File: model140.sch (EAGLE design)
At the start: 12 parts

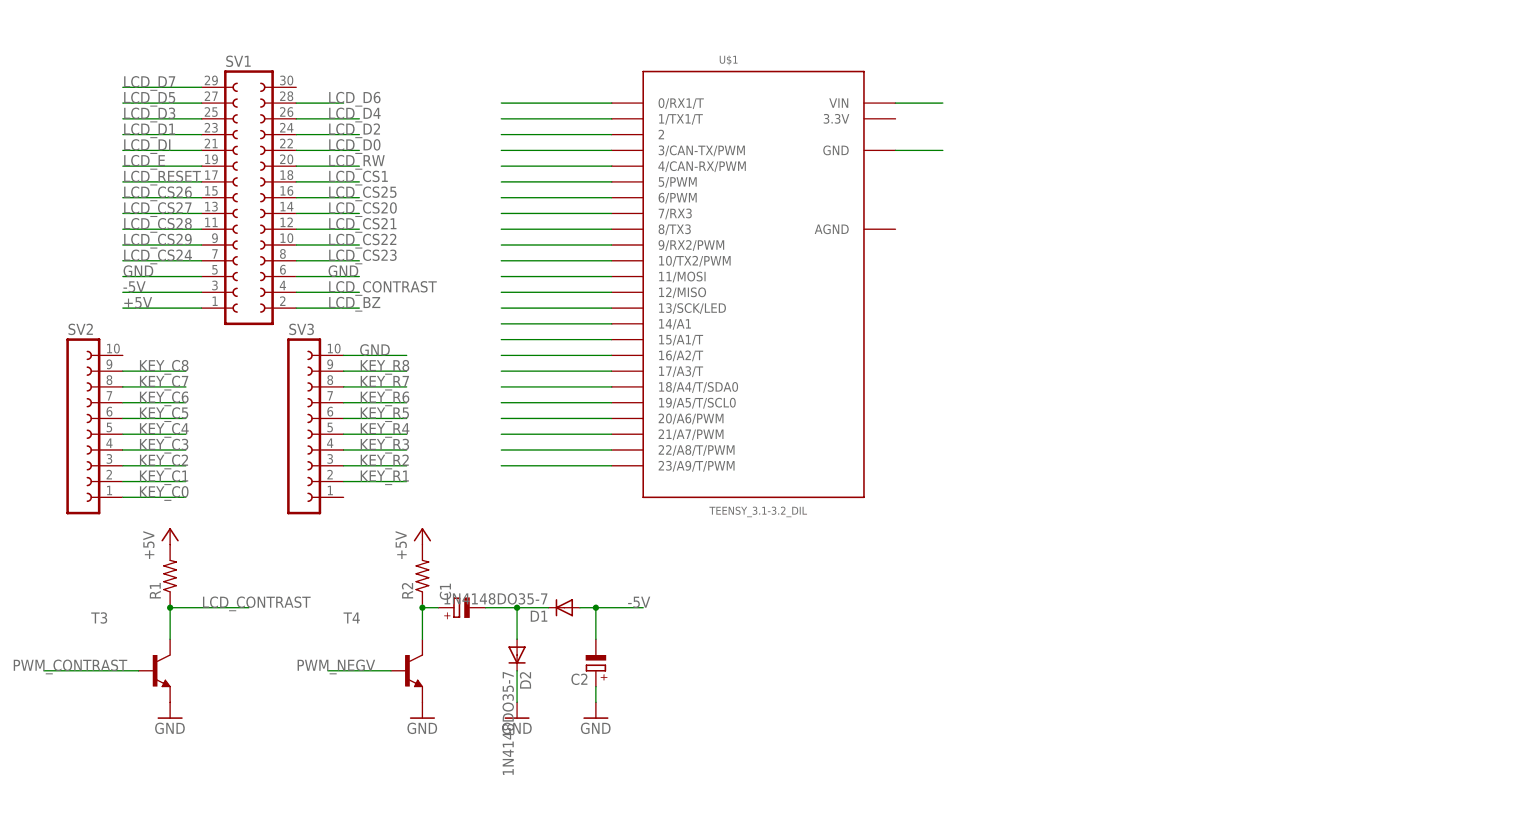
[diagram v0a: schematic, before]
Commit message: pi zero-w version with upduino v2
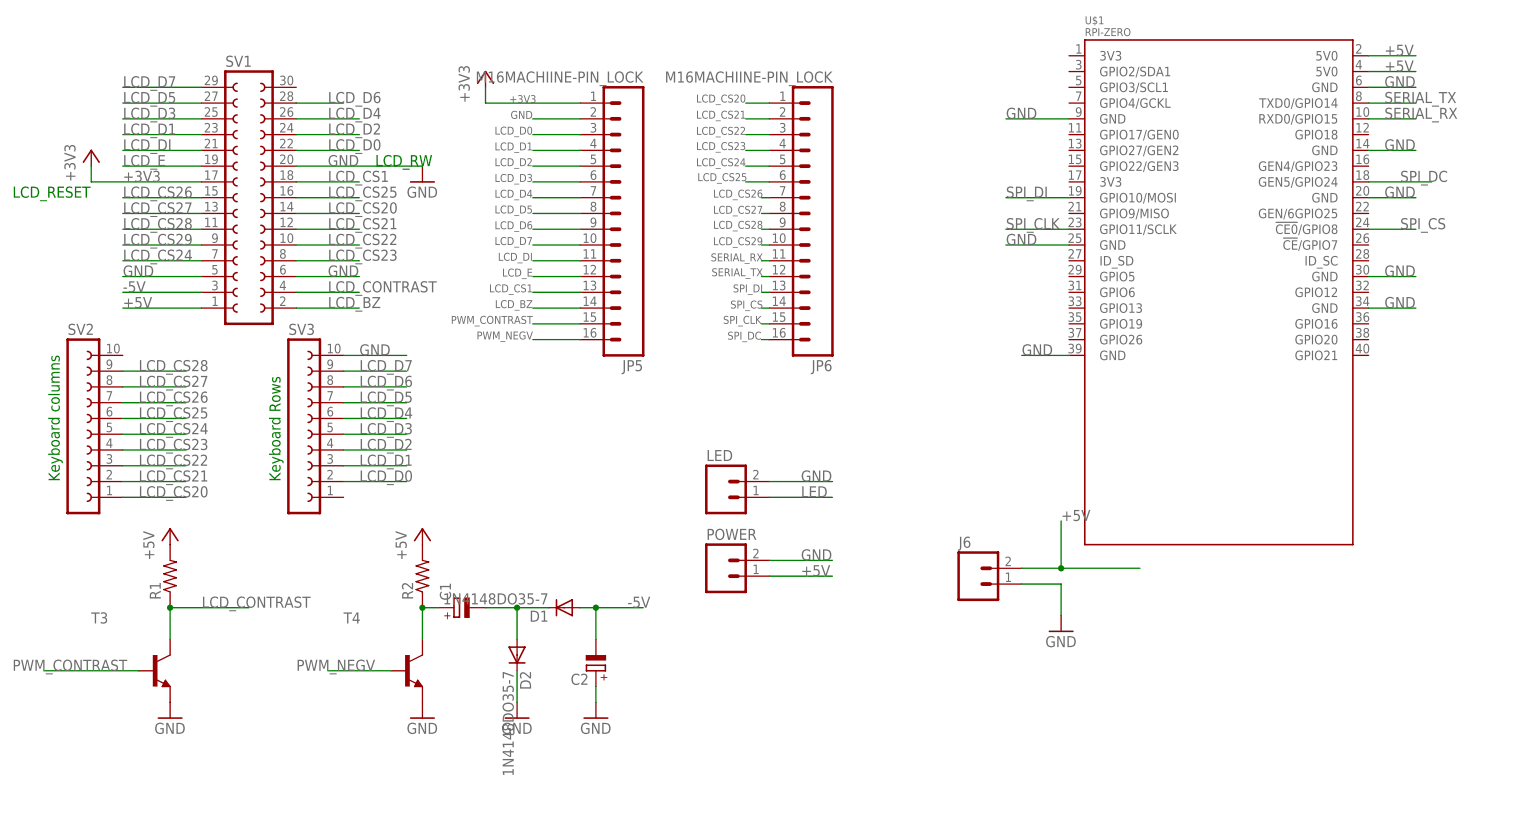
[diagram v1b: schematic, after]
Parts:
- added J6, LED, POWER: (no value), SparkFun-Connectors:M02PTH
- added JP5, JP6: M16MACHIINE-PIN_LOCK, SparkFun-Connectors:M16MACHIINE-PIN_LOCK
- U$1: value TEENSY_3.1-3.2_DIL -> RPI-ZERO; device Teensy_3_and_LC_Series_Boards_v1.4:TEENSY_3.1-3.2_DIL -> rpi-zero:RPI-ZERO
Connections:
- removed net KEY_C0: SV2.1
- removed net KEY_C1: SV2.2
- removed net KEY_C2: SV2.3
- removed net KEY_C3: SV2.4
- removed net KEY_C4: SV2.5
- removed net KEY_C5: SV2.6
- removed net KEY_C6: SV2.7
- removed net KEY_C7: SV2.8
- removed net KEY_C8: SV2.9
- removed net KEY_R1: SV3.2
- removed net KEY_R2: SV3.3
- removed net KEY_R3: SV3.4
- removed net KEY_R4: SV3.5
- removed net KEY_R5: SV3.6
- removed net KEY_R6: SV3.7
- removed net KEY_R7: SV3.8
- removed net KEY_R8: SV3.9
- removed net LCD_RESET: SV1.17
- removed net LCD_RW: SV1.20
- removed net N$1: U$1.0/RX1/T
- removed net N$10: U$1.9/RX2/PWM
- removed net N$11: U$1.10/TX2/PWM
- removed net N$12: U$1.11/MOSI
- removed net N$13: U$1.12/MISO
- removed net N$14: U$1.13/SCK/LED
- removed net N$15: U$1.14/A1
- removed net N$16: U$1.15/A1/T
- removed net N$17: U$1.16/A2/T
- removed net N$18: U$1.17/A3/T
- removed net N$19: U$1.18/A4/T/SDA0
- removed net N$2: U$1.1/TX1/T
- removed net N$20: U$1.19/A5/T/SCL0
- removed net N$21: U$1.20/A6/PWM
- removed net N$22: U$1.21/A7/PWM
- removed net N$23: U$1.22/A8/T/PWM
- removed net N$24: U$1.23/A9/T/PWM
- removed net N$25: U$1.GND
- removed net N$26: U$1.VIN
- removed net N$3: U$1.2
- removed net N$4: U$1.3/CAN-TX/PWM
- removed net N$5: U$1.4/CAN-RX/PWM
- removed net N$6: U$1.5/PWM
- removed net N$7: U$1.6/PWM
- removed net N$8: U$1.7/RX3
- removed net N$9: U$1.8/TX3
- new net +3V3: JP5.1, SV1.17
- new net LED: LED.1
- new net SERIAL_RX: JP6.11, U$1.RXD0/GPIO15
- new net SERIAL_TX: JP6.12, U$1.TXD0/GPIO14
- new net SPI_CLK: JP6.15, U$1.GPIO11/SCLK
- new net SPI_CS: JP6.14, U$1.!CE0!/GPIO8
- new net SPI_DC: JP6.16, U$1.GEN5/GPIO24
- new net SPI_DI: JP6.13, U$1.GPIO10/MOSI
- net +5V: now also J6.2, POWER.1, U$1.5V0@1, U$1.5V0@2
- net GND: now also J6.1, JP5.2, LED.2, POWER.2, SV1.20, U$1.GND@1, U$1.GND@2, U$1.GND@3, U$1.GND@4, U$1.GND@5, U$1.GND@6, U$1.GND@7, U$1.GND@8
- net LCD_BZ: now also JP5.14
- net LCD_CS1: now also JP5.13
- net LCD_CS20: now also JP6.1, SV2.1
- net LCD_CS21: now also JP6.2, SV2.2
- net LCD_CS22: now also JP6.3, SV2.3
- net LCD_CS23: now also JP6.4, SV2.4
- net LCD_CS24: now also JP6.5, SV2.5
- net LCD_CS25: now also JP6.6, SV2.6
- net LCD_CS26: now also JP6.7, SV2.7
- net LCD_CS27: now also JP6.8, SV2.8
- net LCD_CS28: now also JP6.9, SV2.9
- net LCD_CS29: now also JP6.10
- net LCD_D0: now also JP5.3, SV3.2
- net LCD_D1: now also JP5.4, SV3.3
- net LCD_D2: now also JP5.5, SV3.4
- net LCD_D3: now also JP5.6, SV3.5
- net LCD_D4: now also JP5.7, SV3.6
- net LCD_D5: now also JP5.8, SV3.7
- net LCD_D6: now also JP5.9, SV3.8
- net LCD_D7: now also JP5.10, SV3.9
- net LCD_DI: now also JP5.11
- net LCD_E: now also JP5.12
- net PWM_CONTRAST: now also JP5.15
- net PWM_NEGV: now also JP5.16
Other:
- note added: "Keyboard Rows"
- note added: "Keyboard columns"
- note added: "LCD_RESET"
- note added: "LCD_RW"

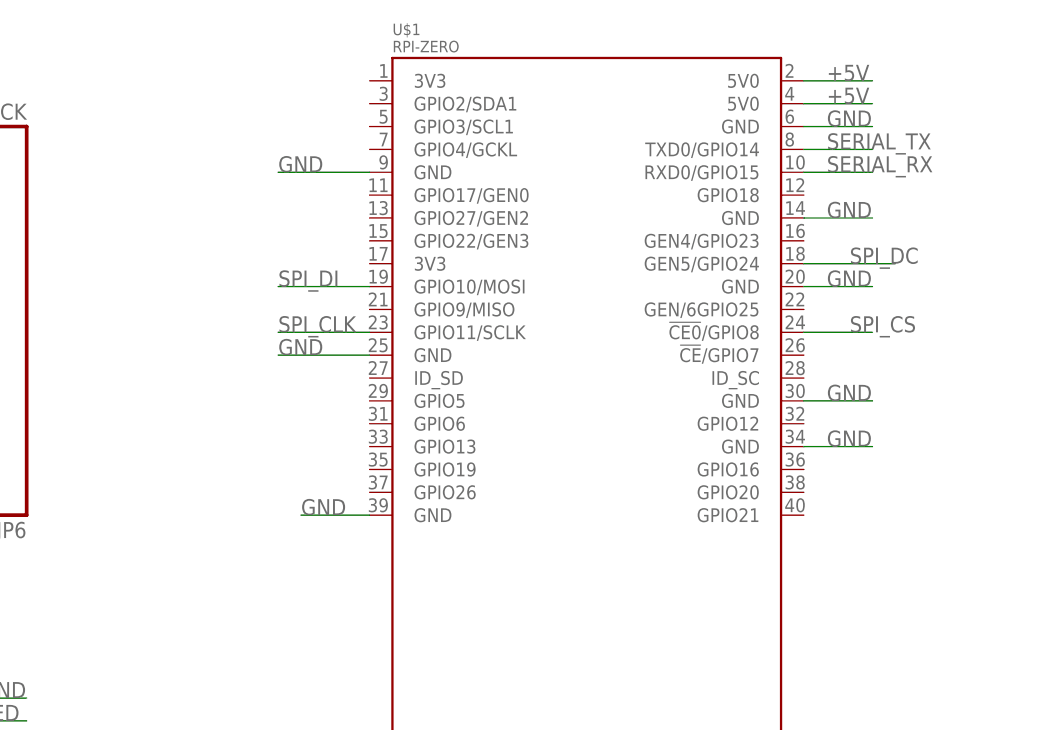
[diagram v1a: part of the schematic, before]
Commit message: add pi-zero header duplicate
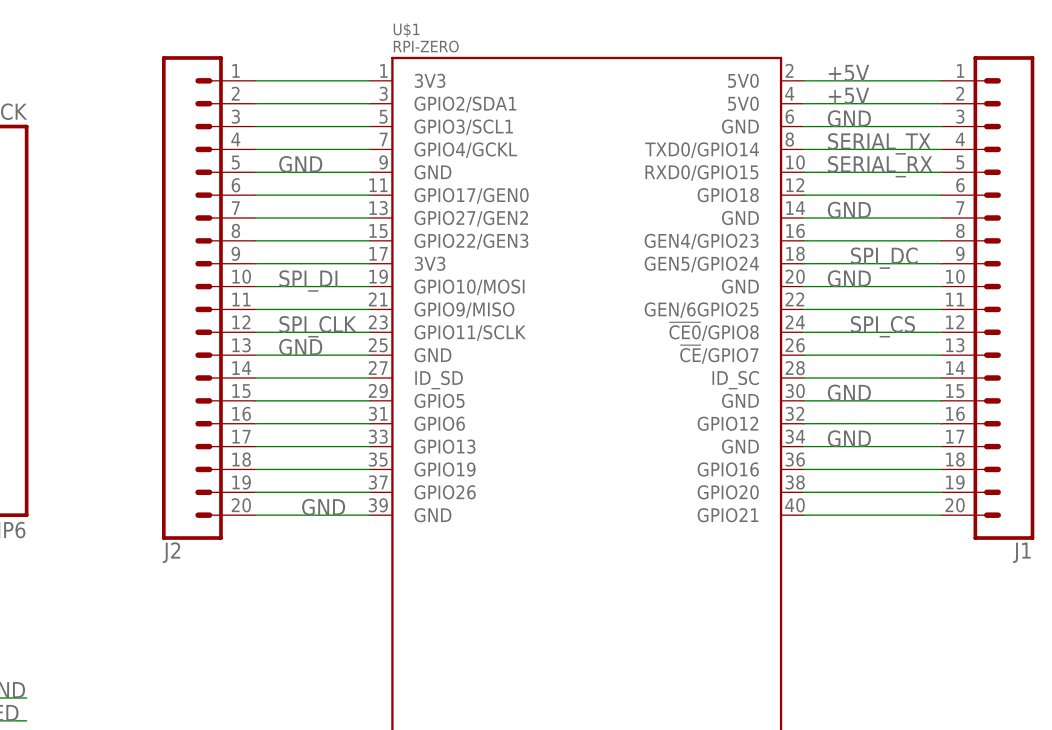
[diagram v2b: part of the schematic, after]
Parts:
- added J1, J2: (no value), SparkFun-Connectors:CONN_20
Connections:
- new net 3V3@1: J2.1, U$1.3V3@1
- new net 3V3@2: J2.9, U$1.3V3@2
- new net N$1: J2.2, U$1.GPIO2/SDA1
- new net N$10: J2.16, U$1.GPIO6
- new net N$11: J2.17, U$1.GPIO13
- new net N$12: J2.18, U$1.GPIO19
- new net N$13: J2.19, U$1.GPIO26
- new net N$14: J1.20, U$1.GPIO21
- new net N$15: J1.19, U$1.GPIO20
- new net N$16: J1.18, U$1.GPIO16
- new net N$17: J1.16, U$1.GPIO12
- new net N$18: J1.14, U$1.ID_SC
- new net N$19: J1.13, U$1.!CE!/GPIO7
- new net N$2: J2.3, U$1.GPIO3/SCL1
- new net N$20: J1.11, U$1.GEN/6GPIO25
- new net N$21: J1.8, U$1.GEN4/GPIO23
- new net N$22: J1.6, U$1.GPIO18
- new net N$3: J2.4, U$1.GPIO4/GCKL
- new net N$4: J2.6, U$1.GPIO17/GEN0
- new net N$5: J2.7, U$1.GPIO27/GEN2
- new net N$6: J2.8, U$1.GPIO22/GEN3
- new net N$7: J2.11, U$1.GPIO9/MISO
- new net N$8: J2.14, U$1.ID_SD
- new net N$9: J2.15, U$1.GPIO5
- net +5V: now also J1.1, J1.2
- net GND: now also J1.10, J1.15, J1.17, J1.3, J1.7, J2.13, J2.20, J2.5
- net SERIAL_RX: now also J1.5
- net SERIAL_TX: now also J1.4
- net SPI_CLK: now also J2.12
- net SPI_CS: now also J1.12
- net SPI_DC: now also J1.9
- net SPI_DI: now also J2.10
